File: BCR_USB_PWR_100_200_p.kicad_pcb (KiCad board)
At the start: 2 copper layers, 13.4 x 21.8 mm, 2 parts, among them CN1 DB9_Female, CN2 UE27AC54100

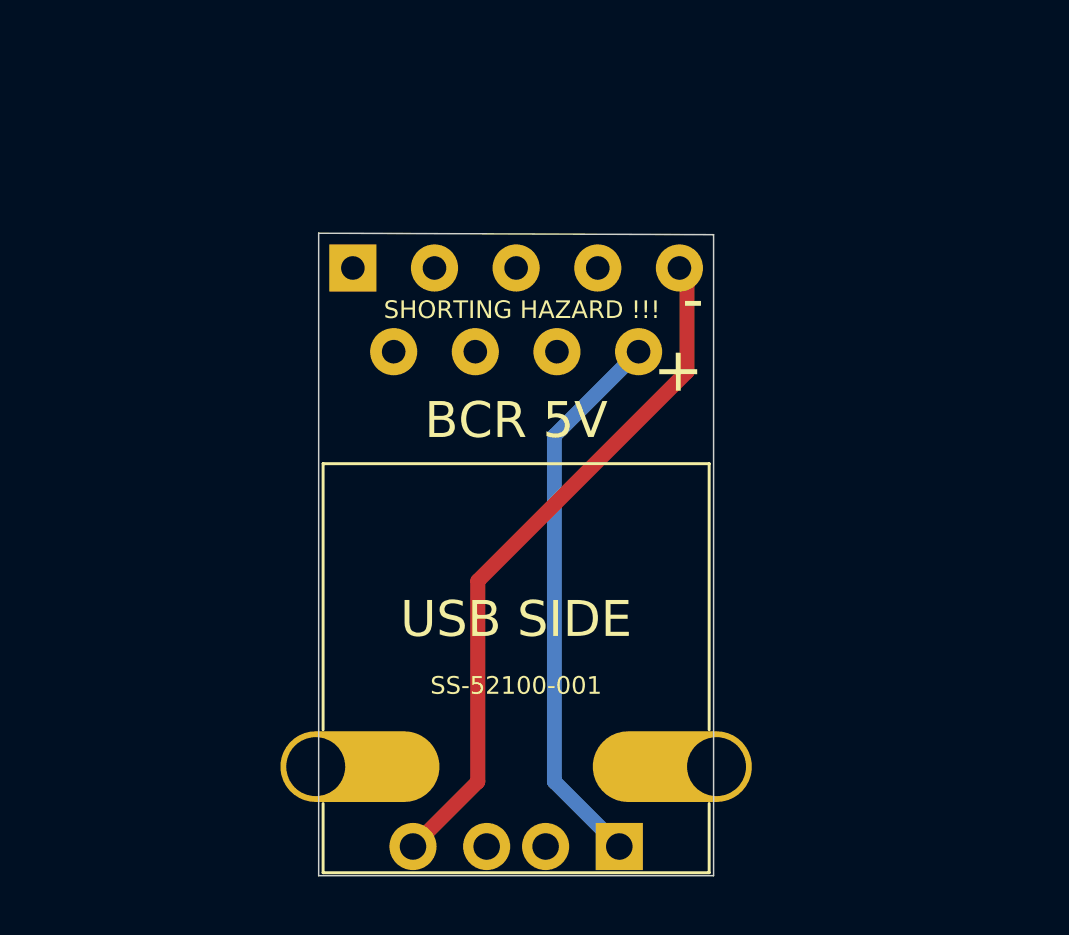
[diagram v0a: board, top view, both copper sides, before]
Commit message: shrink pcbs, 102 pcb, note short hazards
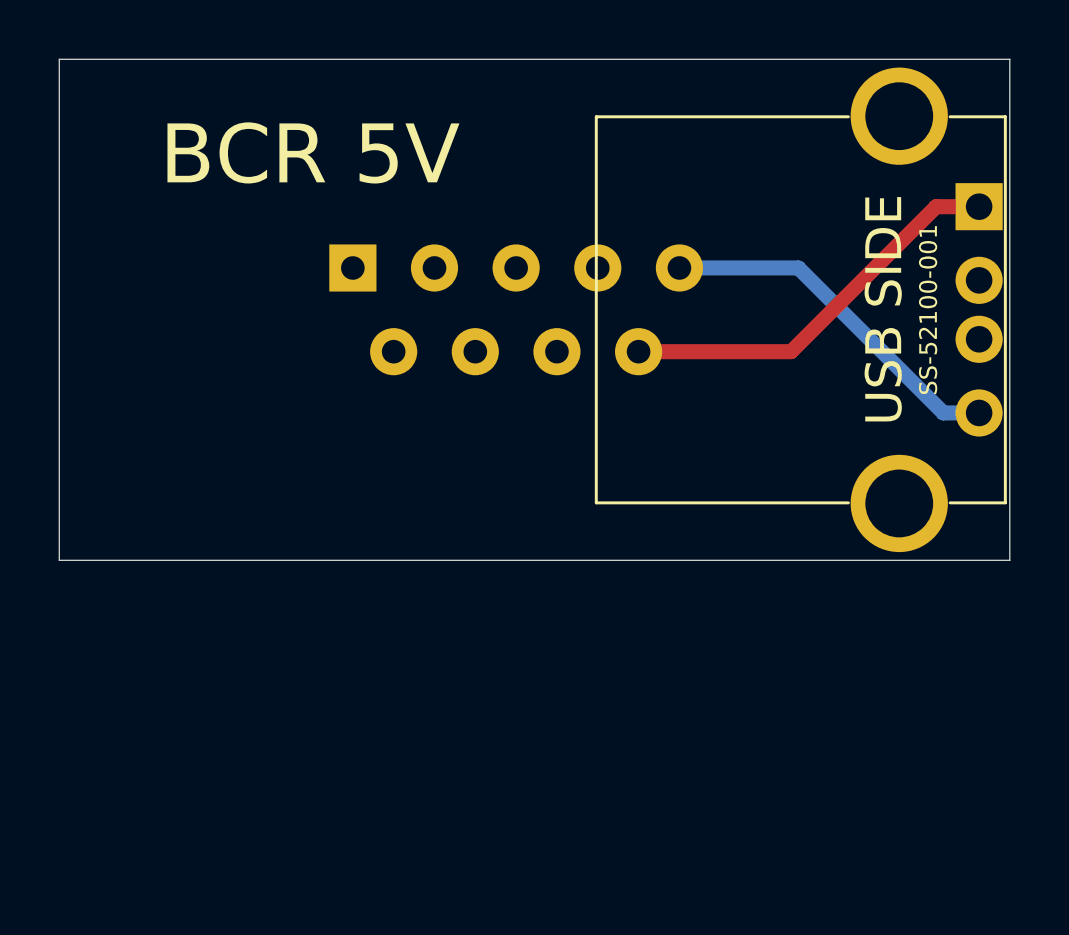
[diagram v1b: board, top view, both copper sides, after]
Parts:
- CN1: footprint 0_LOCAL:A-DF_09_PP-Z_nec -> 0_LOCAL:TE-5207826
- CN2: footprint 0_LOCAL:USB_A_Female_UE27AC54100_cut -> 0_LOCAL:USB_A_Female_UE27AC54100
- moved CN2 20.2 mm to (140.0, 95.8), turned to 270 degrees
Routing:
- net /GND: track 23.6 -> 12.2 mm
- net /+5V: track 18.9 -> 13.6 mm
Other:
- board size 13.4 x 21.8 mm -> 32.2 x 17 mm
- board text added: "5v USB power from BCR port"
- board text added: "TE 5207826"
- board text added: "TRS-80 Model 100 / TANDY 200"
- board text removed: "+"
- board text removed: "-"
- board text removed: "5v USB power"
- board text removed: "A-DF 09 PP/Z"
- board text removed: "NEC PC-8201 / PC-8300"
- board text removed: "SHORTING HAZARD !!!"
- board text removed: "from BCR port"
